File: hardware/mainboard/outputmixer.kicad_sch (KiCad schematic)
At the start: 15 parts, among them J10 MIX, J9 EXT, U12 TL074, U8 TL074

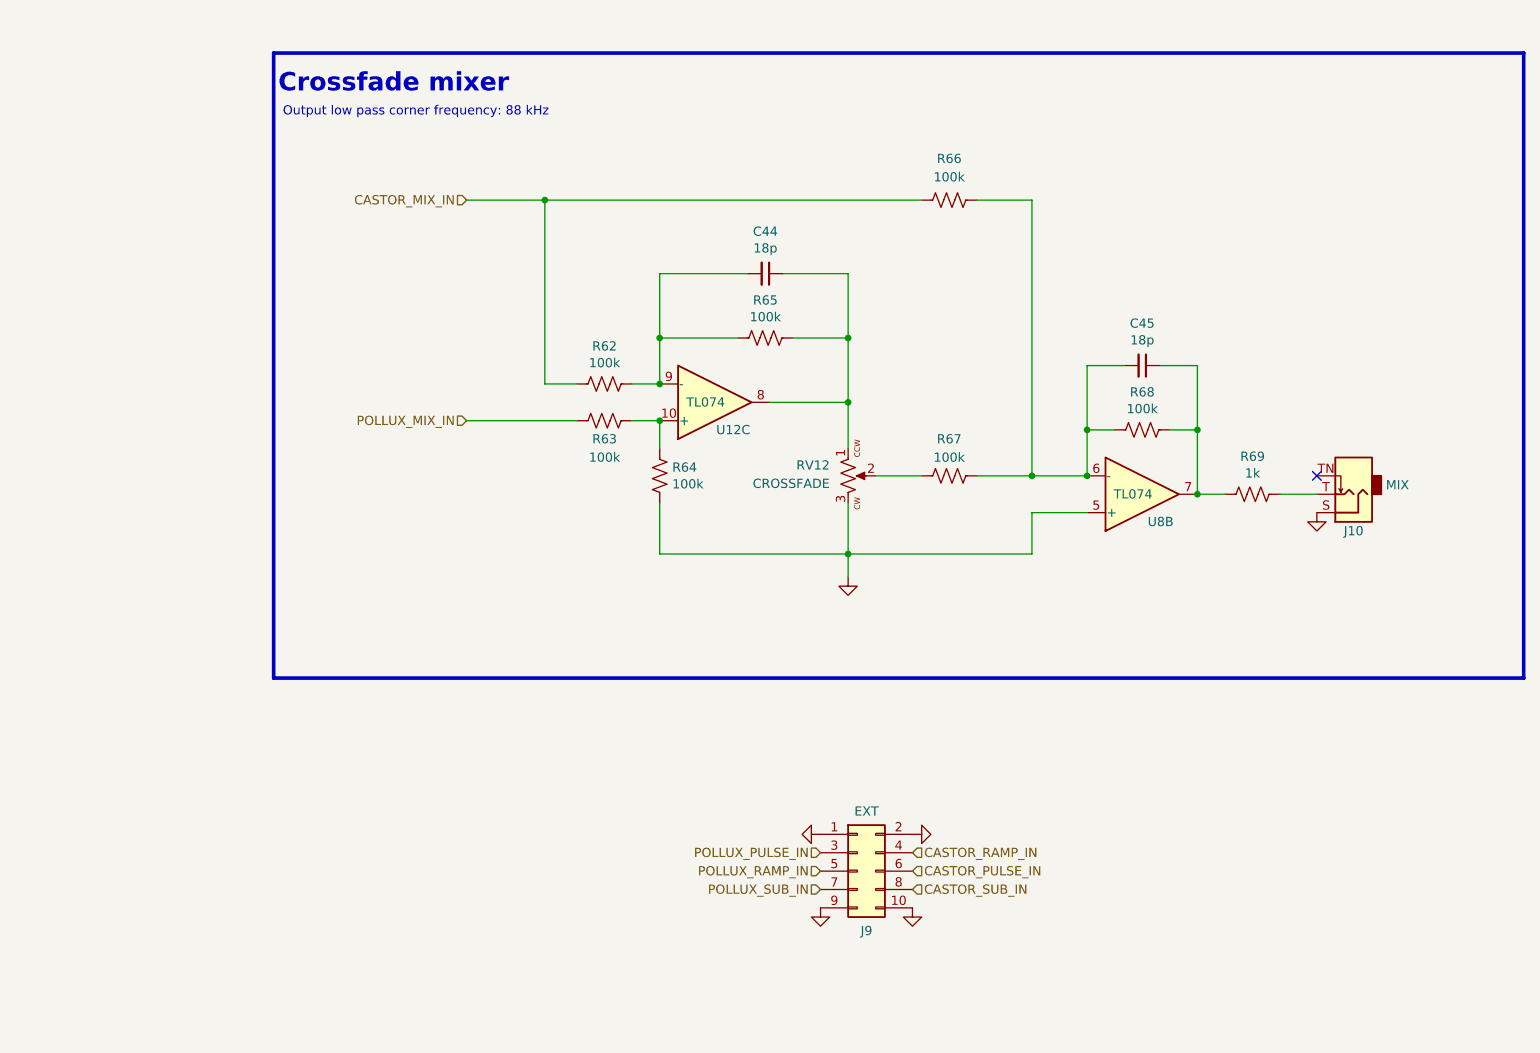
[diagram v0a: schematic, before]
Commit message: A little more schematic cleanup
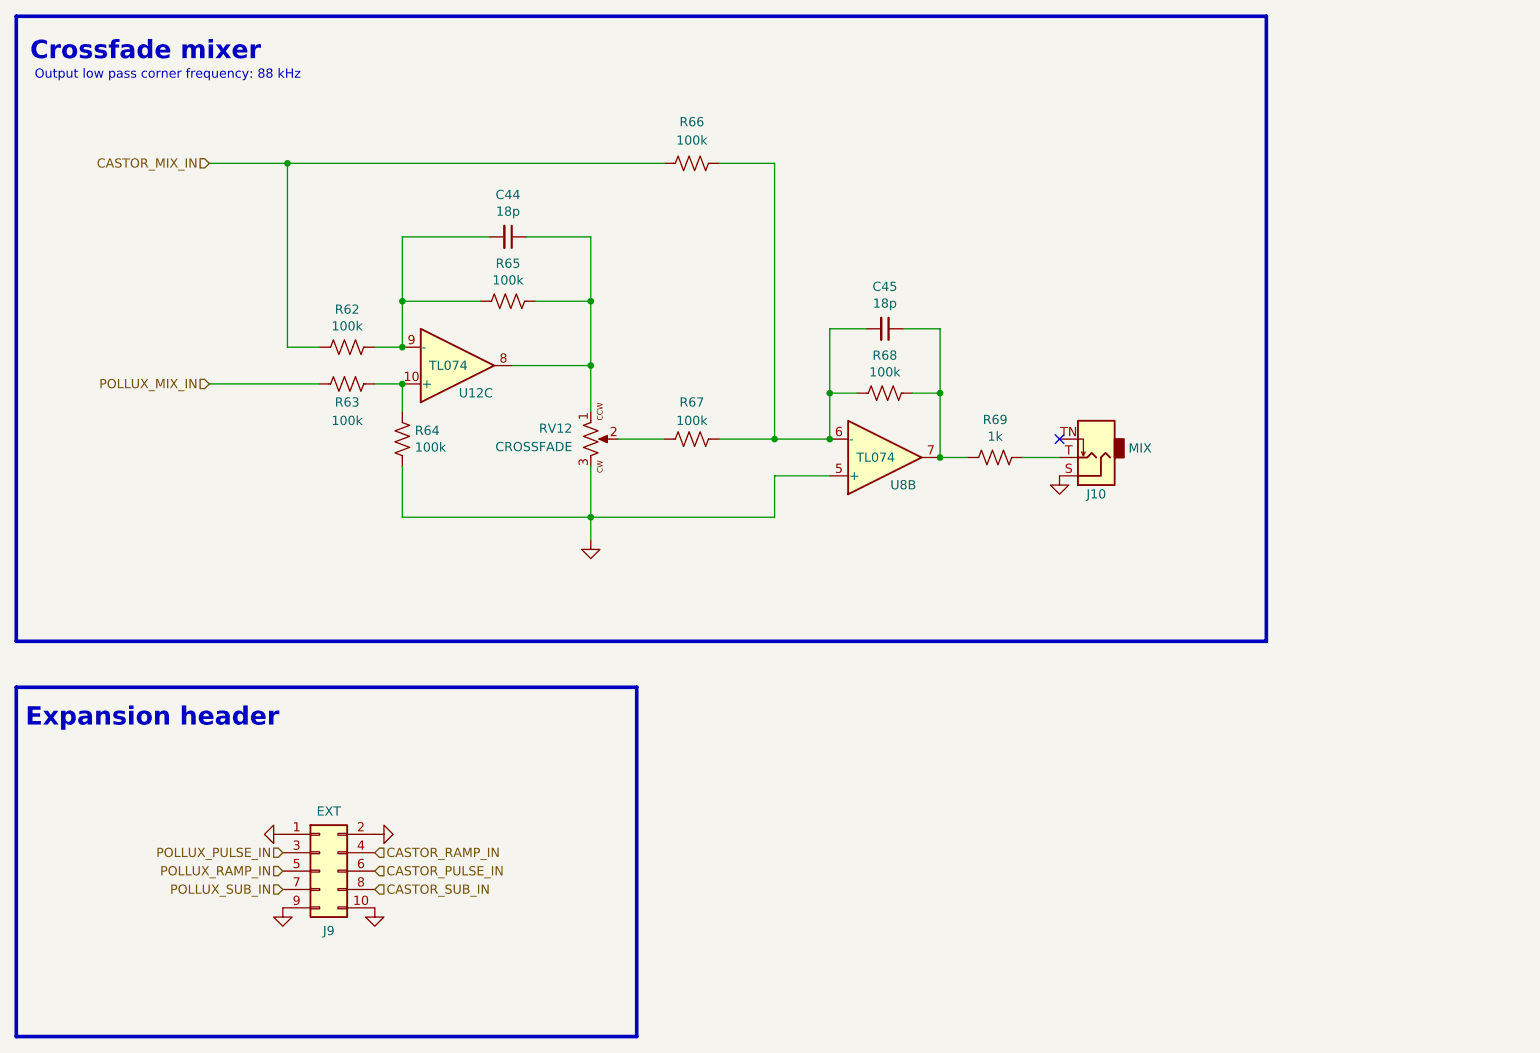
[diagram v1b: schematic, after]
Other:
- note added: "Expansion header"
- moved on the sheet: C44, C45, J10, J9, R62, R63, R64, R65, R66, R67, R68, R69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

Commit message: Finalize resistor mpns
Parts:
- R62, R63, R64, R65, R66, R67, R68: mpn (none) -> RC0402DR-07100KL
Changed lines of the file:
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@@
       (effects (font (size 1.27 1.27)) hide)
     )
-    (property "mpn" "" (id 6) (at 64.135 64.77 0)
+    (property "mpn" "RC0402DR-07100KL" (id 6) (at 64.135 64.77 0)
       (effects (font (size 1.27 1.27)) hide)
     )
@@
       (effects (font (size 1.27 1.27)) hide)
     )
-    (property "mpn" "" (id 6) (at 64.135 69.85 0)
+    (property "mpn" "RC0402DR-07100KL" (id 6) (at 64.135 69.85 0)
       (effects (font (size 1.27 1.27)) hide)
     )
@@
       (effects (font (size 1.27 1.27)) hide)
     )
-    (property "mpn" "" (id 6) (at 71.755 77.47 0)
+    (property "mpn" "RC0402DR-07100KL" (id 6) (at 71.755 77.47 0)
       (effects (font (size 1.27 1.27)) hide)
     )
@@
       (effects (font (size 1.27 1.27)) hide)
     )
-    (property "mpn" "" (id 6) (at 86.36 58.42 0)
+    (property "mpn" "RC0402DR-07100KL" (id 6) (at 86.36 58.42 0)
       (effects (font (size 1.27 1.27)) hide)
     )
@@
       (effects (font (size 1.27 1.27)) hide)
     )
-    (property "mpn" "" (id 6) (at 111.76 39.37 0)
+    (property "mpn" "RC0402DR-07100KL" (id 6) (at 111.76 39.37 0)
       (effects (font (size 1.27 1.27)) hide)
     )
@@
       (effects (font (size 1.27 1.27)) hide)
     )
-    (property "mpn" "" (id 6) (at 111.76 77.47 0)
+    (property "mpn" "RC0402DR-07100KL" (id 6) (at 111.76 77.47 0)
       (effects (font (size 1.27 1.27)) hide)
     )
@@
       (effects (font (size 1.27 1.27)) hide)
     )
-    (property "mpn" "" (id 6) (at 138.43 71.12 0)
-      (effects (font (size 1.27 1.27)) hide)
-    )
+    (property "mpn" "RC0402DR-07100KL" (id 6) (at 138.43 71.12 0)
+      (effects (font (size 1.27 1.27)) hide)
+    )

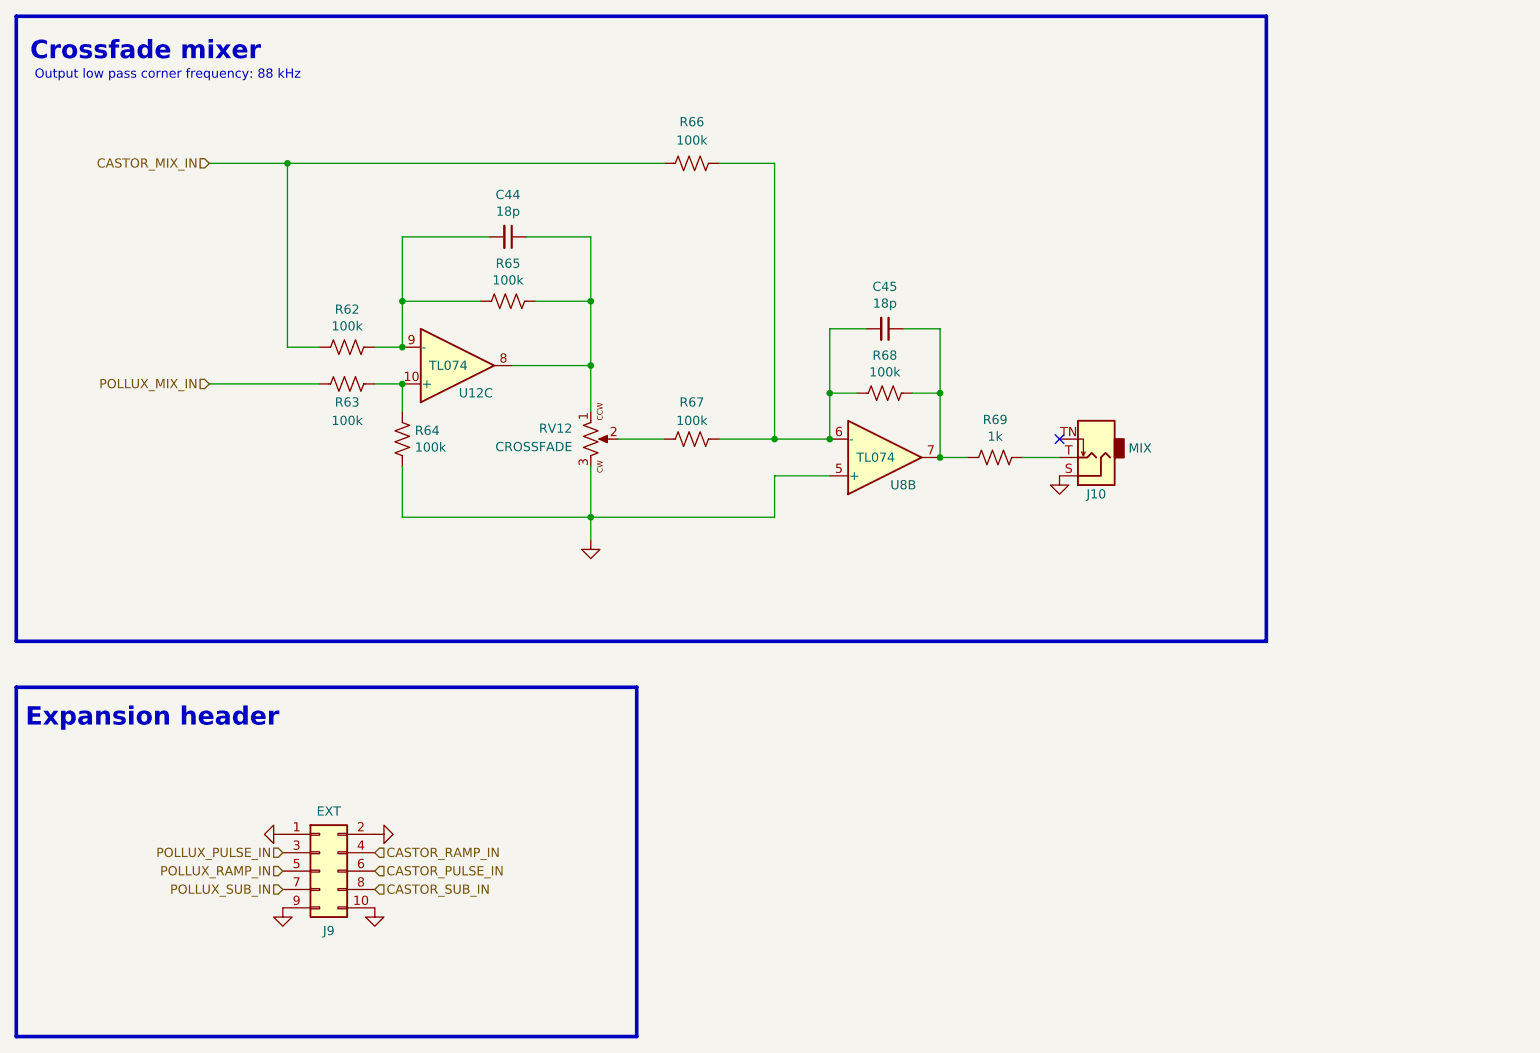
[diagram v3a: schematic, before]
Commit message: hardware: add rating field to schematic
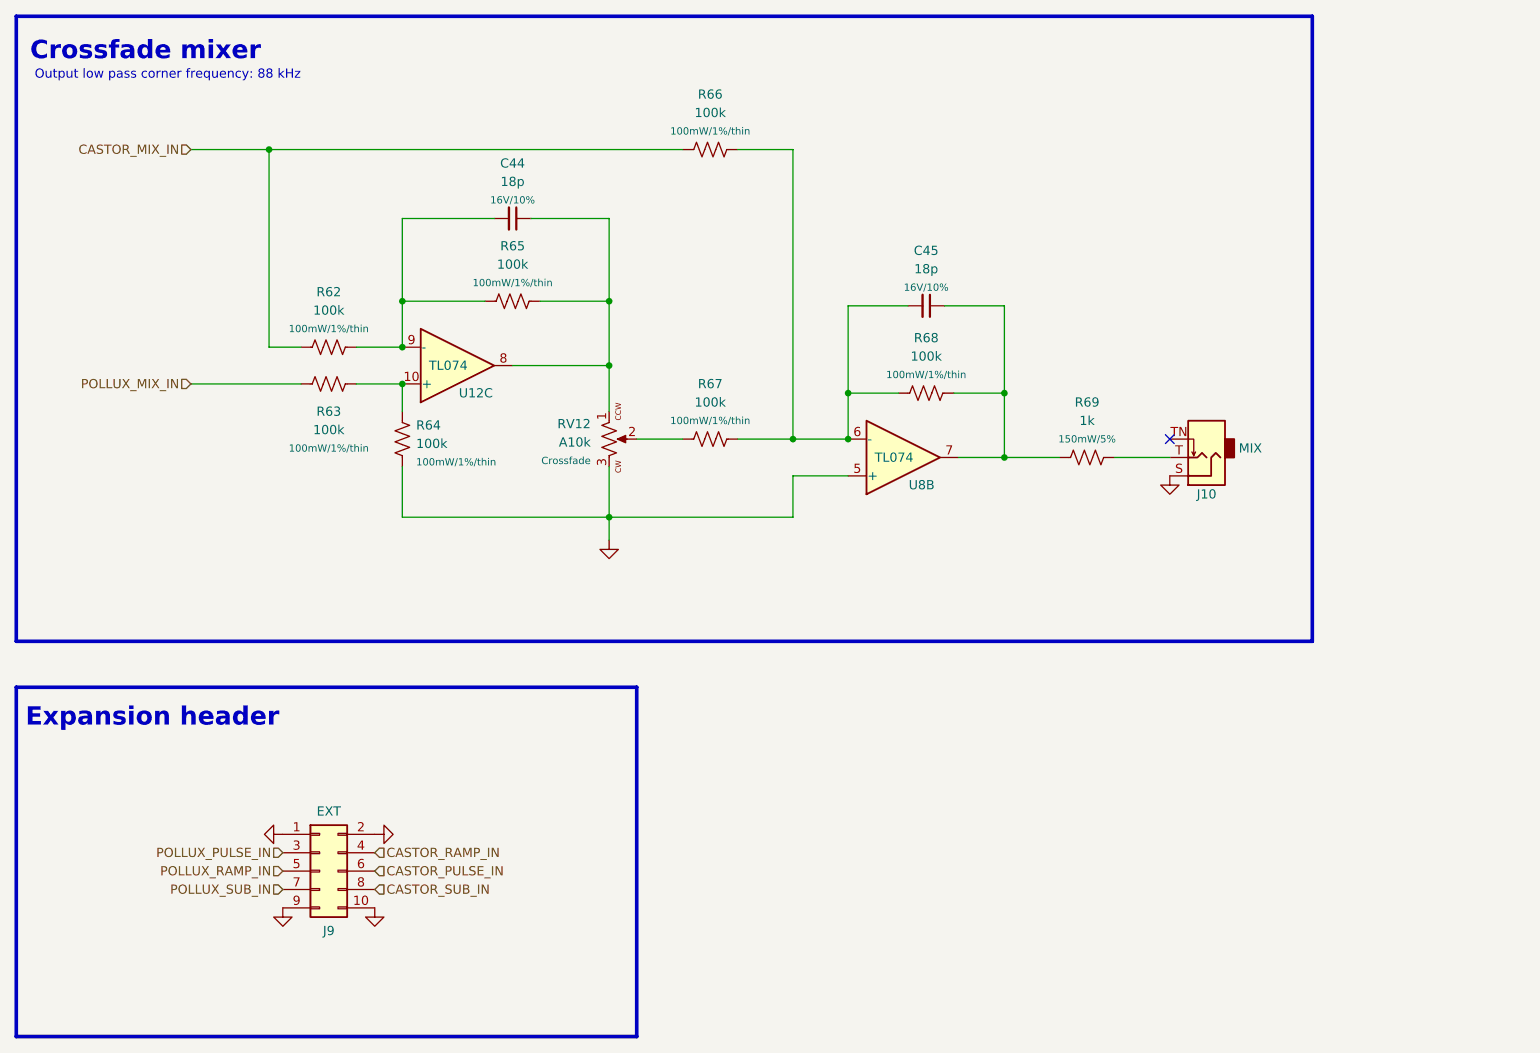
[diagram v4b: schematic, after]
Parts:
- C44, C45: Rating (none) -> 16V/10%
- R62, R63, R64, R65, R66, R67, R68: Rating (none) -> 100mW/1%/thin
- R69: Rating (none) -> 150mW/5%
- RV12: value CROSSFADE -> A10k; Rating (none) -> Crossfade
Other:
- moved on the sheet: C44, C45, J10, R62, R63, R65, R66, R67, R68, R69, RV12, U8B

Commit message: hardware: fixup schematic fields
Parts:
- C44, C45: MPN (none) -> CL05C180JB5NNNC; Notes (none) -> Eurorack level audio filter; Reqs Eurorack level audio filter, 16 V -> (none); finalized yes -> (none); mpn CL05C180JB5NNNC -> (none)
- J10: MPN (none) -> WQP-WQP518MA; finalized yes -> (none); mpn WQP-WQP518MA -> (none)
- J9: MPN (none) -> 3220-10-0300-00; finalized yes -> (none); mpn 3220-10-0300-00 -> (none)
- R62, R63, R64, R65, R66, R67, R68: MPN (none) -> RC0402DR-07100KL; Notes (none) -> Eurorack level audio; Reqs Eurorack level audio, 1%, 100 mW, thin film -> (none); mpn RC0402DR-07100KL -> (none)
- R69: MPN (none) -> MCT06030C1001FP500, ERA-3AEB102V; Notes (none) -> Eurorack level audio, output impedance; Reqs Output impedance, 5%, 150 mW, thin film -> (none); mpn MCT06030C1001FP500, ERA-3AEB102V -> (none)
- RV12: MPN (none) -> https://www.thonk.co.uk/shop/vertical-b10k-10k-linear/; Notes (none) -> 10k, linear taper, 6.35 mm round shaft, 15 mm height; Reqs 10k, linear taper, 6.35 mm round shaft, 15 mm height -> (none); finalized yes -> (none); mpn https://www.thonk.co.uk/shop/vertical-b10k-10k-linear/ -> (none)
- U12, U8: MPN (none) -> TL074CPW; finalized yes -> (none); mpn TL074CPW -> (none)

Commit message: hardware: use winterbloom footprints for C, R, and L
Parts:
- C44, C45: footprint Capacitor_SMD:C_0402_1005Metric_Pad0.74x0.62mm_HandSolder -> winterbloom:C_0402_HandSolder
- R62, R63, R64, R65, R66, R67, R68: footprint Resistor_SMD:R_0402_1005Metric_Pad0.72x0.64mm_HandSolder -> winterbloom:R_0402_HandSolder
- R69: footprint Resistor_SMD:R_0603_1608Metric_Pad0.98x0.95mm_HandSolder -> winterbloom:R_0603_HandSolder
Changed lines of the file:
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@@
     (property "Reference" "R62" (id 0) (at 61.595 57.15 90))
     (property "Value" "100k" (id 1) (at 61.595 59.69 90))
-    (property "Footprint" "Resistor_SMD:R_0402_1005Metric_Pad0.72x0.64mm_HandSolder" (id 2) (at 61.341 65.786 90)
+    (property "Footprint" "winterbloom:R_0402_HandSolder" (id 2) (at 61.341 65.786 90)
       (effects (font (size 1.27 1.27)) hide)
     )
@@
     (property "Reference" "R63" (id 0) (at 61.595 73.66 90))
     (property "Value" "100k" (id 1) (at 61.595 76.2 90))
-    (property "Footprint" "Resistor_SMD:R_0402_1005Metric_Pad0.72x0.64mm_HandSolder" (id 2) (at 61.341 70.866 90)
+    (property "Footprint" "winterbloom:R_0402_HandSolder" (id 2) (at 61.341 70.866 90)
       (effects (font (size 1.27 1.27)) hide)
     )
@@
       (effects (font (size 1.27 1.27)) (justify right))
     )
-    (property "Footprint" "Resistor_SMD:R_0402_1005Metric_Pad0.72x0.64mm_HandSolder" (id 2) (at 70.739 77.216 90)
+    (property "Footprint" "winterbloom:R_0402_HandSolder" (id 2) (at 70.739 77.216 90)
       (effects (font (size 1.27 1.27)) hide)
     )
@@
     (property "Reference" "R65" (id 0) (at 86.995 50.8 90))
     (property "Value" "100k" (id 1) (at 86.995 53.34 90))
-    (property "Footprint" "Resistor_SMD:R_0402_1005Metric_Pad0.72x0.64mm_HandSolder" (id 2) (at 87.249 57.404 90)
+    (property "Footprint" "winterbloom:R_0402_HandSolder" (id 2) (at 87.249 57.404 90)
       (effects (font (size 1.27 1.27)) hide)
     )
@@
     (property "Reference" "R66" (id 0) (at 114.3 29.845 90))
     (property "Value" "100k" (id 1) (at 114.3 32.385 90))
-    (property "Footprint" "Resistor_SMD:R_0402_1005Metric_Pad0.72x0.64mm_HandSolder" (id 2) (at 114.554 36.449 90)
+    (property "Footprint" "winterbloom:R_0402_HandSolder" (id 2) (at 114.554 36.449 90)
       (effects (font (size 1.27 1.27)) hide)
     )
@@
     (property "Reference" "C44" (id 0) (at 86.9886 39.37 90))
     (property "Value" "18p" (id 1) (at 86.9886 41.91 90))
-    (property "Footprint" "Capacitor_SMD:C_0402_1005Metric_Pad0.74x0.62mm_HandSolder" (id 2) (at 86.995 46.99 0)
+    (property "Footprint" "winterbloom:C_0402_HandSolder" (id 2) (at 86.995 46.99 0)
       (effects (font (size 1.27 1.27)) hide)
     )
@@
     (property "Reference" "R67" (id 0) (at 114.3 69.85 90))
     (property "Value" "100k" (id 1) (at 114.3 72.39 90))
-    (property "Footprint" "Resistor_SMD:R_0402_1005Metric_Pad0.72x0.64mm_HandSolder" (id 2) (at 114.554 76.454 90)
+    (property "Footprint" "winterbloom:R_0402_HandSolder" (id 2) (at 114.554 76.454 90)
       (effects (font (size 1.27 1.27)) hide)
     )
@@
     (property "Reference" "R68" (id 0) (at 144.145 63.5 90))
     (property "Value" "100k" (id 1) (at 144.145 66.04 90))
-    (property "Footprint" "Resistor_SMD:R_0402_1005Metric_Pad0.72x0.64mm_HandSolder" (id 2) (at 144.399 70.104 90)
+    (property "Footprint" "winterbloom:R_0402_HandSolder" (id 2) (at 144.399 70.104 90)
       (effects (font (size 1.27 1.27)) hide)
     )
@@
     (property "Reference" "R69" (id 0) (at 166.37 72.39 90))
     (property "Value" "1k" (id 1) (at 166.37 74.93 90))
-    (property "Footprint" "Resistor_SMD:R_0603_1608Metric_Pad0.98x0.95mm_HandSolder" (id 2) (at 166.624 78.994 90)
+    (property "Footprint" "winterbloom:R_0603_HandSolder" (id 2) (at 166.624 78.994 90)
       (effects (font (size 1.27 1.27)) hide)
     )
@@
     (property "Reference" "C45" (id 0) (at 144.1386 51.435 90))
     (property "Value" "18p" (id 1) (at 144.1386 53.975 90))
-    (property "Footprint" "Capacitor_SMD:C_0402_1005Metric_Pad0.74x0.62mm_HandSolder" (id 2) (at 144.145 59.055 0)
-      (effects (font (size 1.27 1.27)) hide)
-    )
+    (property "Footprint" "winterbloom:C_0402_HandSolder" (id 2) (at 144.145 59.055 0)
+      (effects (font (size 1.27 1.27)) hide)
+    )
